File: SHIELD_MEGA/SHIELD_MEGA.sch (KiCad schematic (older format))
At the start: 1 part

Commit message: GND routing
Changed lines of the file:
@@
 Text Label 7750 3300 0    50   ~ 0
 GND
+Wire Wire Line
+	7750 3300 8050 3300
 $EndSCHEMATC

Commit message: Adding new labels
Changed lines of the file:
@@
 	8050 1150 7300 1150
 $Sheet
-S 1050 2800 1250 1500
+S 1050 2650 1250 1500
 U 6197A5F1
 F0 "Receiver" 50
@@
 $EndSheet
 $Sheet
-S 8050 2950 950  850
+S 8050 2700 950  850
 U 6197A819
 F0 "GPS" 50
 F1 "gps_module.sch" 50
 $EndSheet
-Text HLabel 8050 3300 2    50   Input ~ 0
+Text HLabel 8050 2850 2    50   Input ~ 0
 GND
-Text Label 7750 3300 0    50   ~ 0
+Text Label 7750 2850 0    50   ~ 0
 GND
 Wire Wire Line
+	7750 2850 8050 2850
+Text HLabel 8050 3300 2    50   Input ~ 0
+5V
+Text HLabel 8050 3000 2    50   Input ~ 0
+RX
+Text HLabel 8050 3150 2    50   Input ~ 0
+TX
+Text Label 7750 3300 0    50   ~ 0
+5V
+Wire Wire Line
 	7750 3300 8050 3300
+Text HLabel 7300 3000 0    50   Input ~ 0
+RX
+Text HLabel 7300 3150 0    50   Input ~ 0
+TX
+Wire Wire Line
+	7300 3000 8050 3000
+Wire Wire Line
+	7300 3150 8050 3150
 $EndSCHEMATC

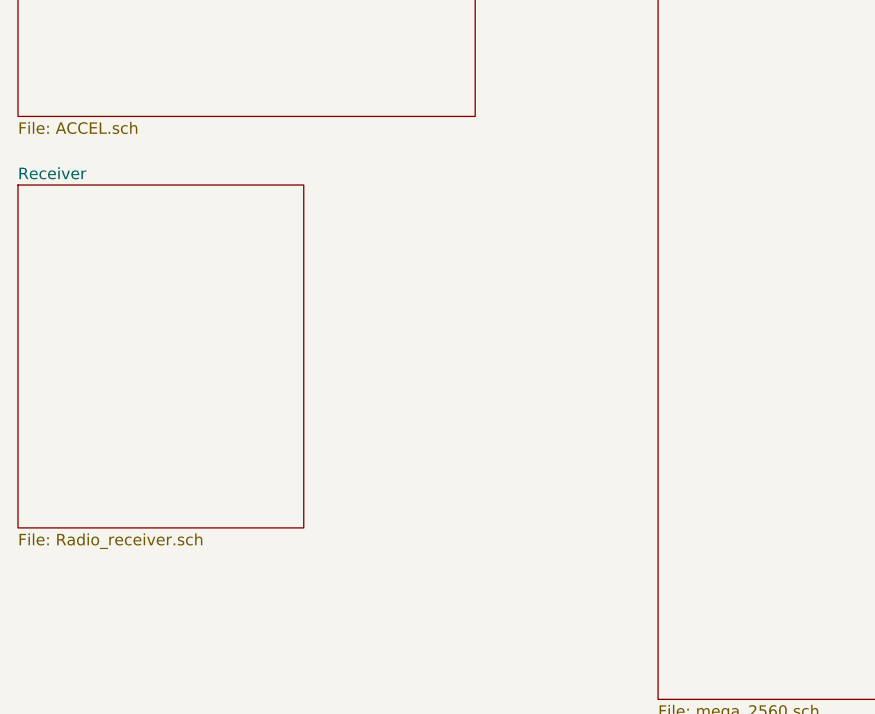
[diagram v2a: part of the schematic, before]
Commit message: Adding radio receiver bus
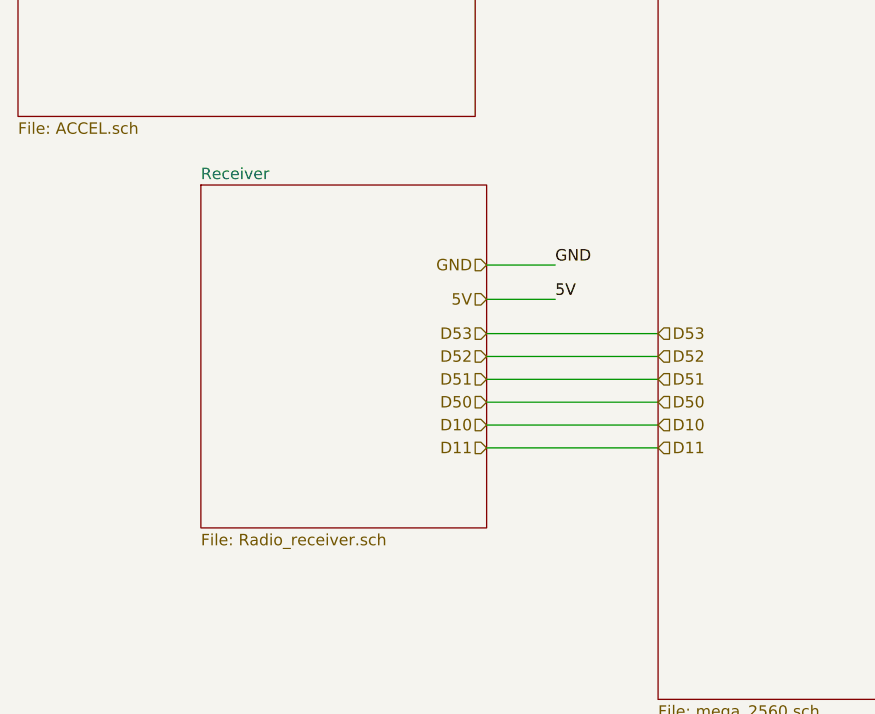
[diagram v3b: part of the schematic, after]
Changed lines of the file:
@@
 	8050 1150 7300 1150
 $Sheet
-S 1050 2650 1250 1500
+S 1850 2650 1250 1500
 U 6197A5F1
 F0 "Receiver" 50
@@
 Wire Wire Line
 	7300 3150 8050 3150
+Text HLabel 3100 3000 0    50   Input ~ 0
+GND
+Text HLabel 3100 3150 0    50   Input ~ 0
+5V
+Text Label 3400 3000 0    50   ~ 0
+GND
+Wire Wire Line
+	3400 3000 3100 3000
+Wire Wire Line
+	3100 3150 3400 3150
+Text Label 3400 3150 0    50   ~ 0
+5V
+Text HLabel 3100 3300 0    50   Input ~ 0
+D53
+Text HLabel 3100 3400 0    50   Input ~ 0
+D52
+Text HLabel 3100 3500 0    50   Input ~ 0
+D51
+Text HLabel 3100 3600 0    50   Input ~ 0
+D50
+Text HLabel 3100 3800 0    50   Input ~ 0
+D11
+Text HLabel 3100 3700 0    50   Input ~ 0
+D10
+Text HLabel 3850 3300 2    50   Input ~ 0
+D53
+Text HLabel 3850 3400 2    50   Input ~ 0
+D52
+Text HLabel 3850 3500 2    50   Input ~ 0
+D51
+Text HLabel 3850 3600 2    50   Input ~ 0
+D50
+Text HLabel 3850 3700 2    50   Input ~ 0
+D10
+Text HLabel 3850 3800 2    50   Input ~ 0
+D11
+Wire Wire Line
+	3100 3300 3850 3300
+Wire Wire Line
+	3850 3400 3100 3400
+Wire Wire Line
+	3100 3500 3850 3500
+Wire Wire Line
+	3850 3600 3100 3600
+Wire Wire Line
+	3100 3700 3850 3700
+Wire Wire Line
+	3850 3800 3100 3800
 $EndSCHEMATC
